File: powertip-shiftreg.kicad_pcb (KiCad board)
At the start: 2 copper layers, 50.8 x 73.7 mm, 9 parts, among them P1 CONN_01X05, P2 CONN_01X03, U1 ICL7660, U2 74HC164, U3 HD44780

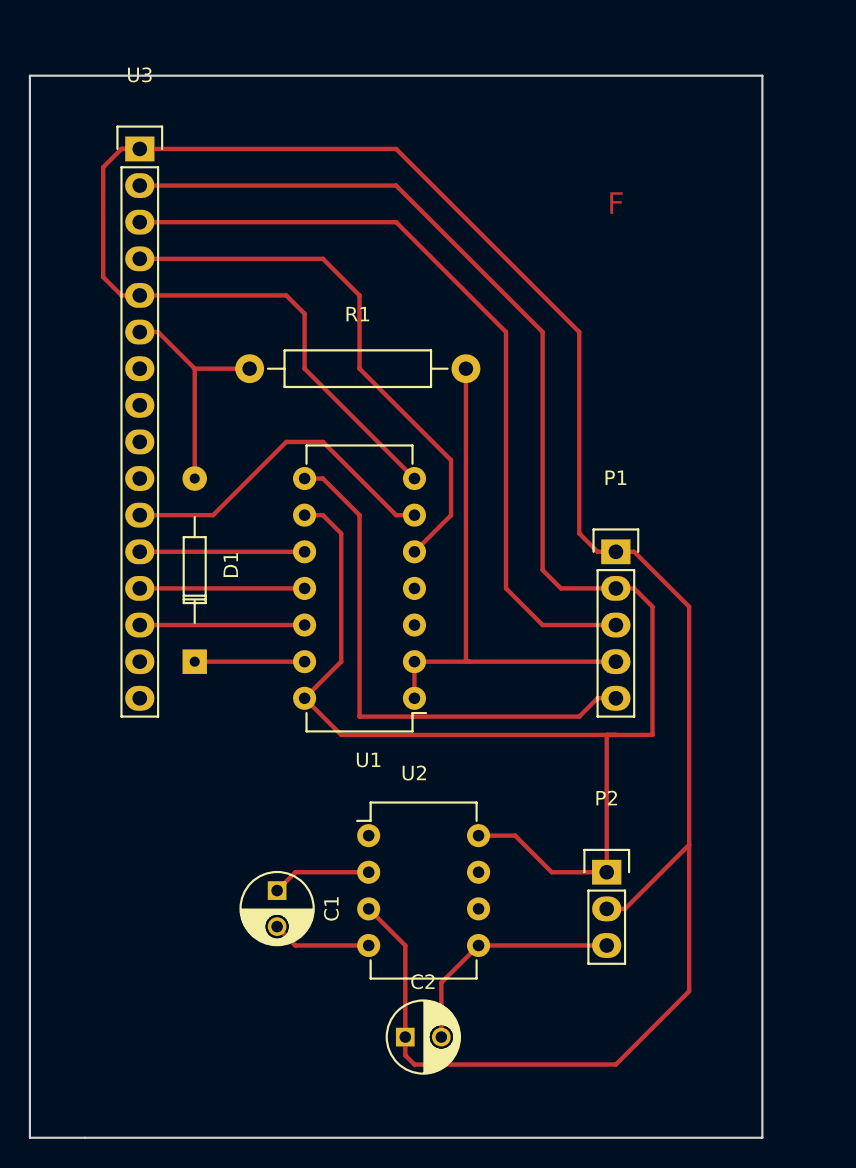
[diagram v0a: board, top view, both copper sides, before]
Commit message: - Board ist jetzt unter dem Display plaziert. - 3er Stecker hat jetzt VCC+, Contrast, VCC-
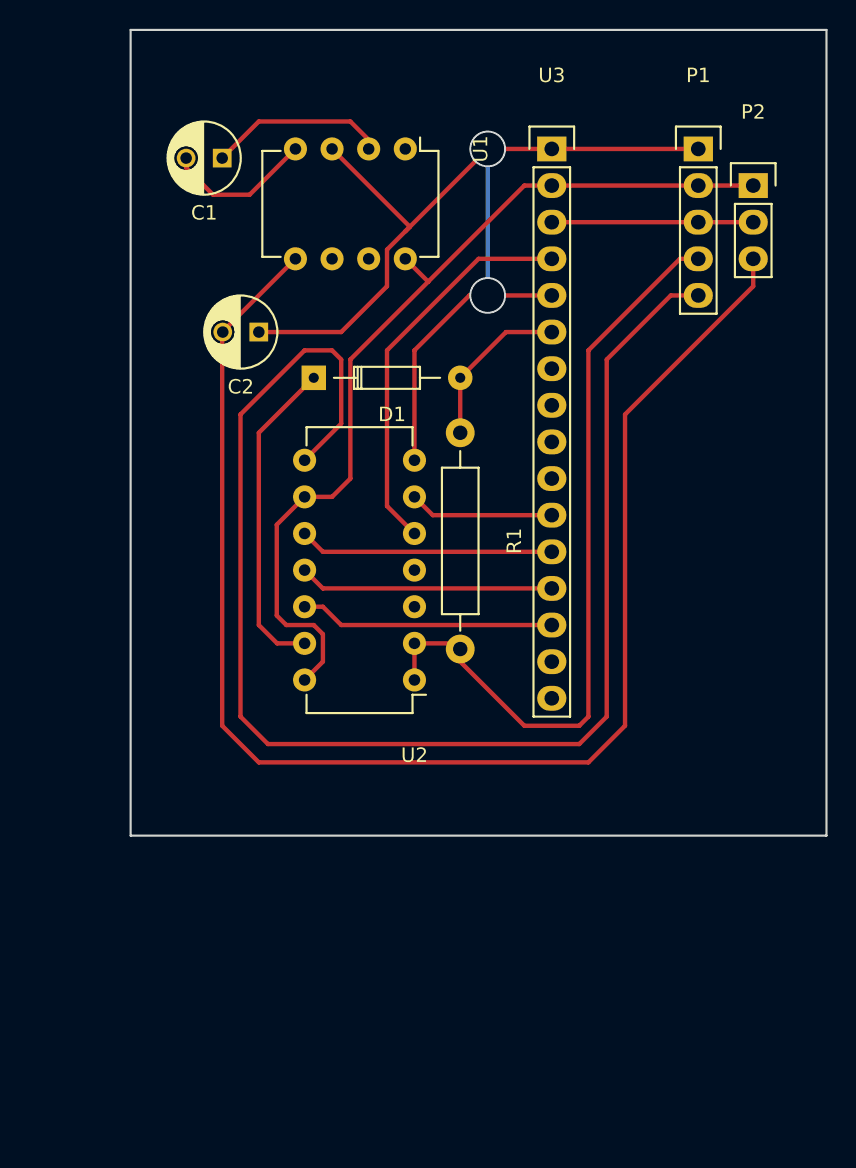
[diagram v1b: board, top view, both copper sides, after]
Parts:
- moved C1 50.9 mm to (134.0, 76.8), turned to 180 degrees
- moved C2 49.9 mm to (136.5, 88.9), turned to 180 degrees
- moved P2 48.7 mm to (170.8, 78.7)
- moved U1 47.7 mm to (146.7, 76.2), turned to 270 degrees
- moved U3 28.6 mm to (156.8, 76.2)
- moved P1 28.5 mm to (167.0, 76.2)
- moved D1 20.2 mm to (140.3, 92.1), turned to 0 degrees
- moved R1 15.3 mm to (150.5, 95.9), turned to 270 degrees
- moved U2 1.27 mm to (147.3, 113.0)
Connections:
- P1 pad 3: Net-(P1-Pad3) -> /Contrast
- P2 pad 2: GND -> /Contrast
- U3 pad 3: Net-(P1-Pad3) -> /Contrast
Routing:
- net GND: track 168.5 -> 74.2 mm, vias 0 -> 2
- net Net-(C2-Pad2): track 16.3 -> 100.6 mm
- net +5V: track 127.1 -> 63.6 mm
- net Net-(P1-Pad5): track 37.1 -> 98.0 mm
- net Net-(P1-Pad3): track 55.0 -> 0.00 mm
- net Net-(P1-Pad4): track 37.1 -> 53.4 mm
- net Net-(D1-Pad1): track 7.62 -> 22.4 mm
- net /Contrast: track 0.00 -> 14.0 mm
- net Net-(U2-Pad6): track 23.3 -> 10.1 mm
- net Net-(U2-Pad5): track 37.8 -> 27.5 mm
- net Net-(U2-Pad11): track 11.4 -> 17.7 mm
- net Net-(U2-Pad12): track 11.4 -> 17.7 mm
- net Net-(U2-Pad10): track 11.4 -> 17.7 mm
- net Net-(C1-Pad1): track 6.88 -> 12.4 mm
- net Net-(D1-Pad2): track 16.3 -> 11.5 mm
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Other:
- board size 50.8 x 73.7 mm -> 48.3 x 55.9 mm
- board text removed: "F"
